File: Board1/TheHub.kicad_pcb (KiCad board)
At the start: 2 copper layers, 195.6 x 195.6 mm, 55 parts, among them J1 ARM_ADC_1, J10 SCIENCE + WHEELS POWER CONN, J11 RFD900, J12 I2C_1 Test Point, J13 I2C_2 Test Point, J14 ARDUINO NANO LEFT, J15 GPIO Test, J16 I2C_3 Test Point, J17 12V OUT, J18 7.4V IN, J19 ANALOG SENSORS, J2 ARM_ADC_2, J20 GPS, J21 COMPASS, J22 ARDUINO NANO RIGHT, J23 NucleoRight, J3 ARM_PWM_OUT, J4 ARM POWER CONN, J5 NucleoLeft, J6 SCI_ADC_1, J7 SCIENCE_PWM_OUT, J8 12V MAIN POWER, J9 WHEEL_ADC_1, U1 PRE-PCA9685, U2 PRE-ADS1115, U3 PRE-ADS1115, U4 PRE-PCA9685, U5 PRE-ADS1115, U6 TL1963, U7 LM340MP-5.0, U9 PRE-ADS1115

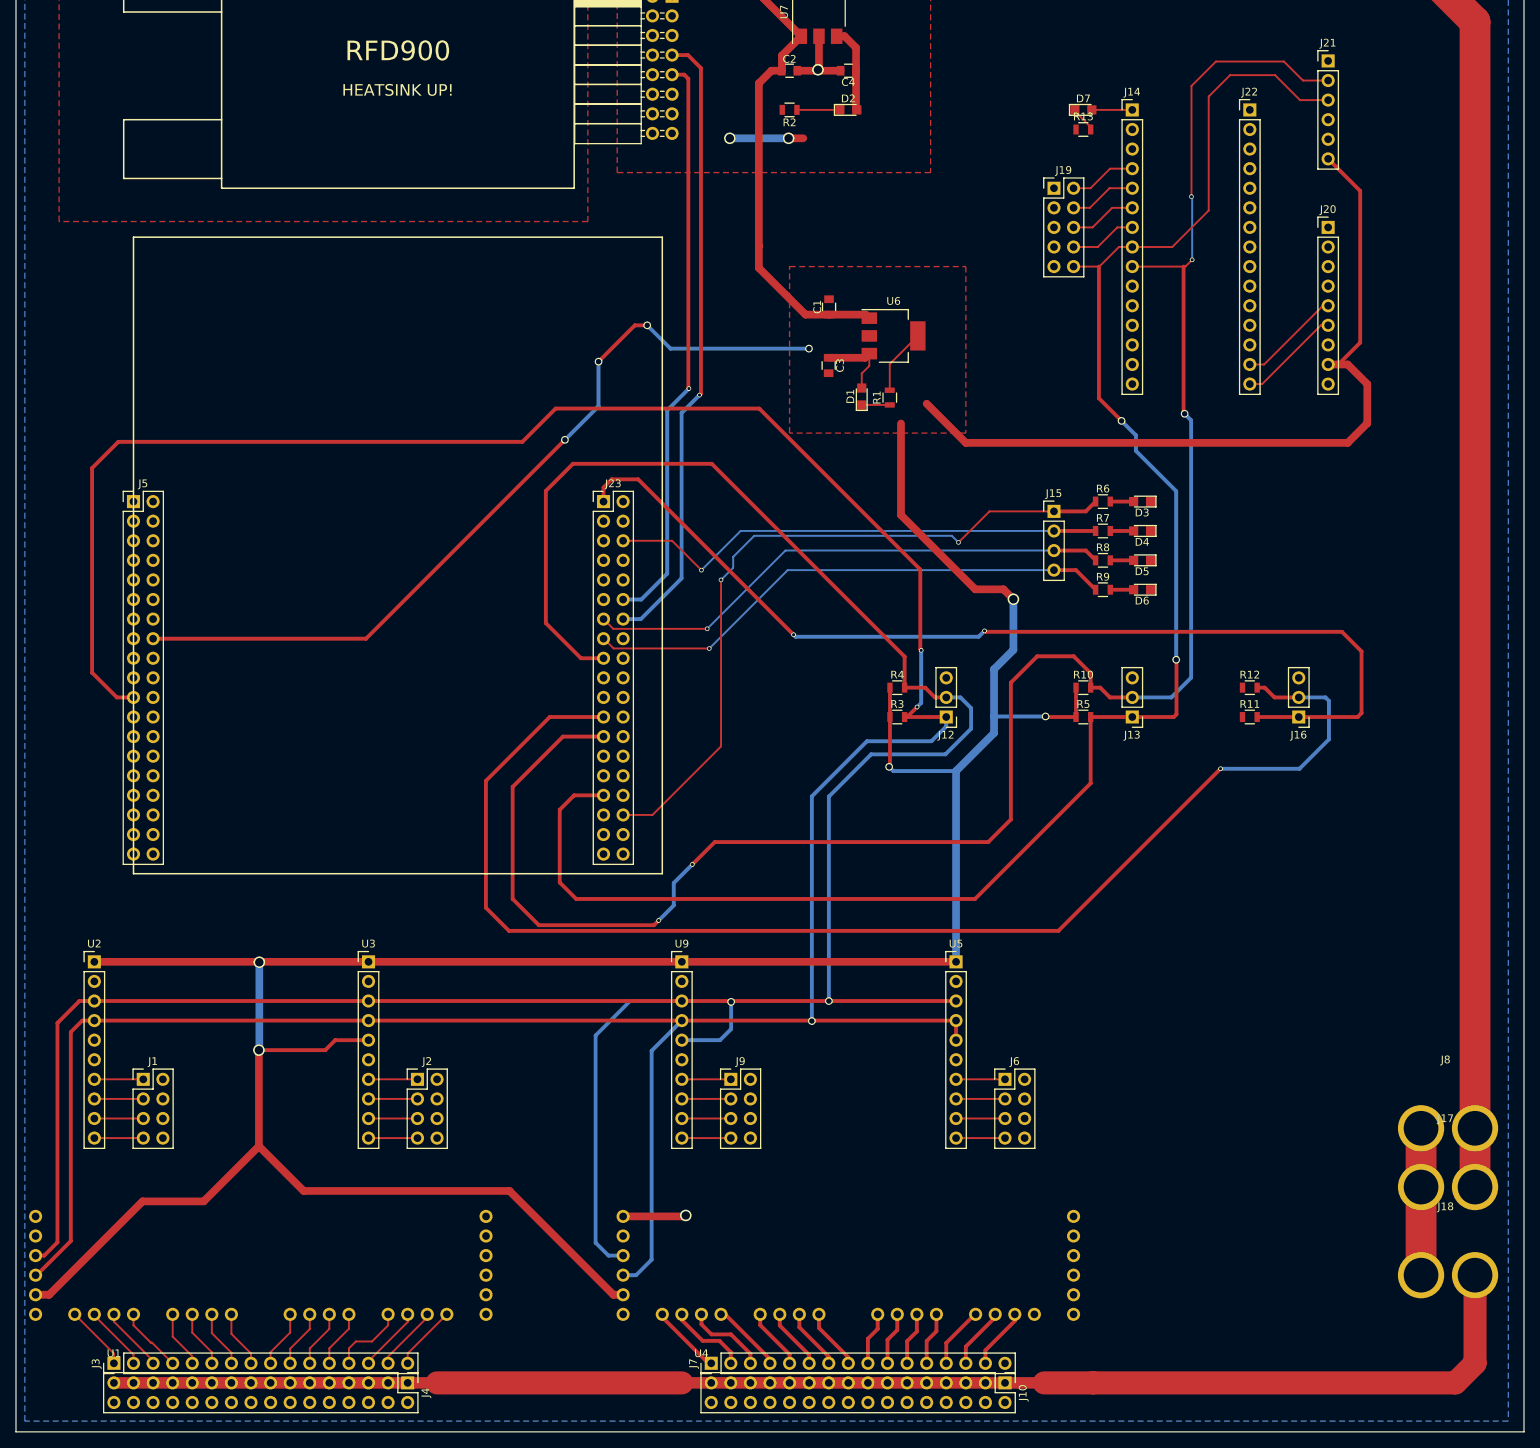
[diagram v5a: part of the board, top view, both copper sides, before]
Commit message: Add silkscreen labeling
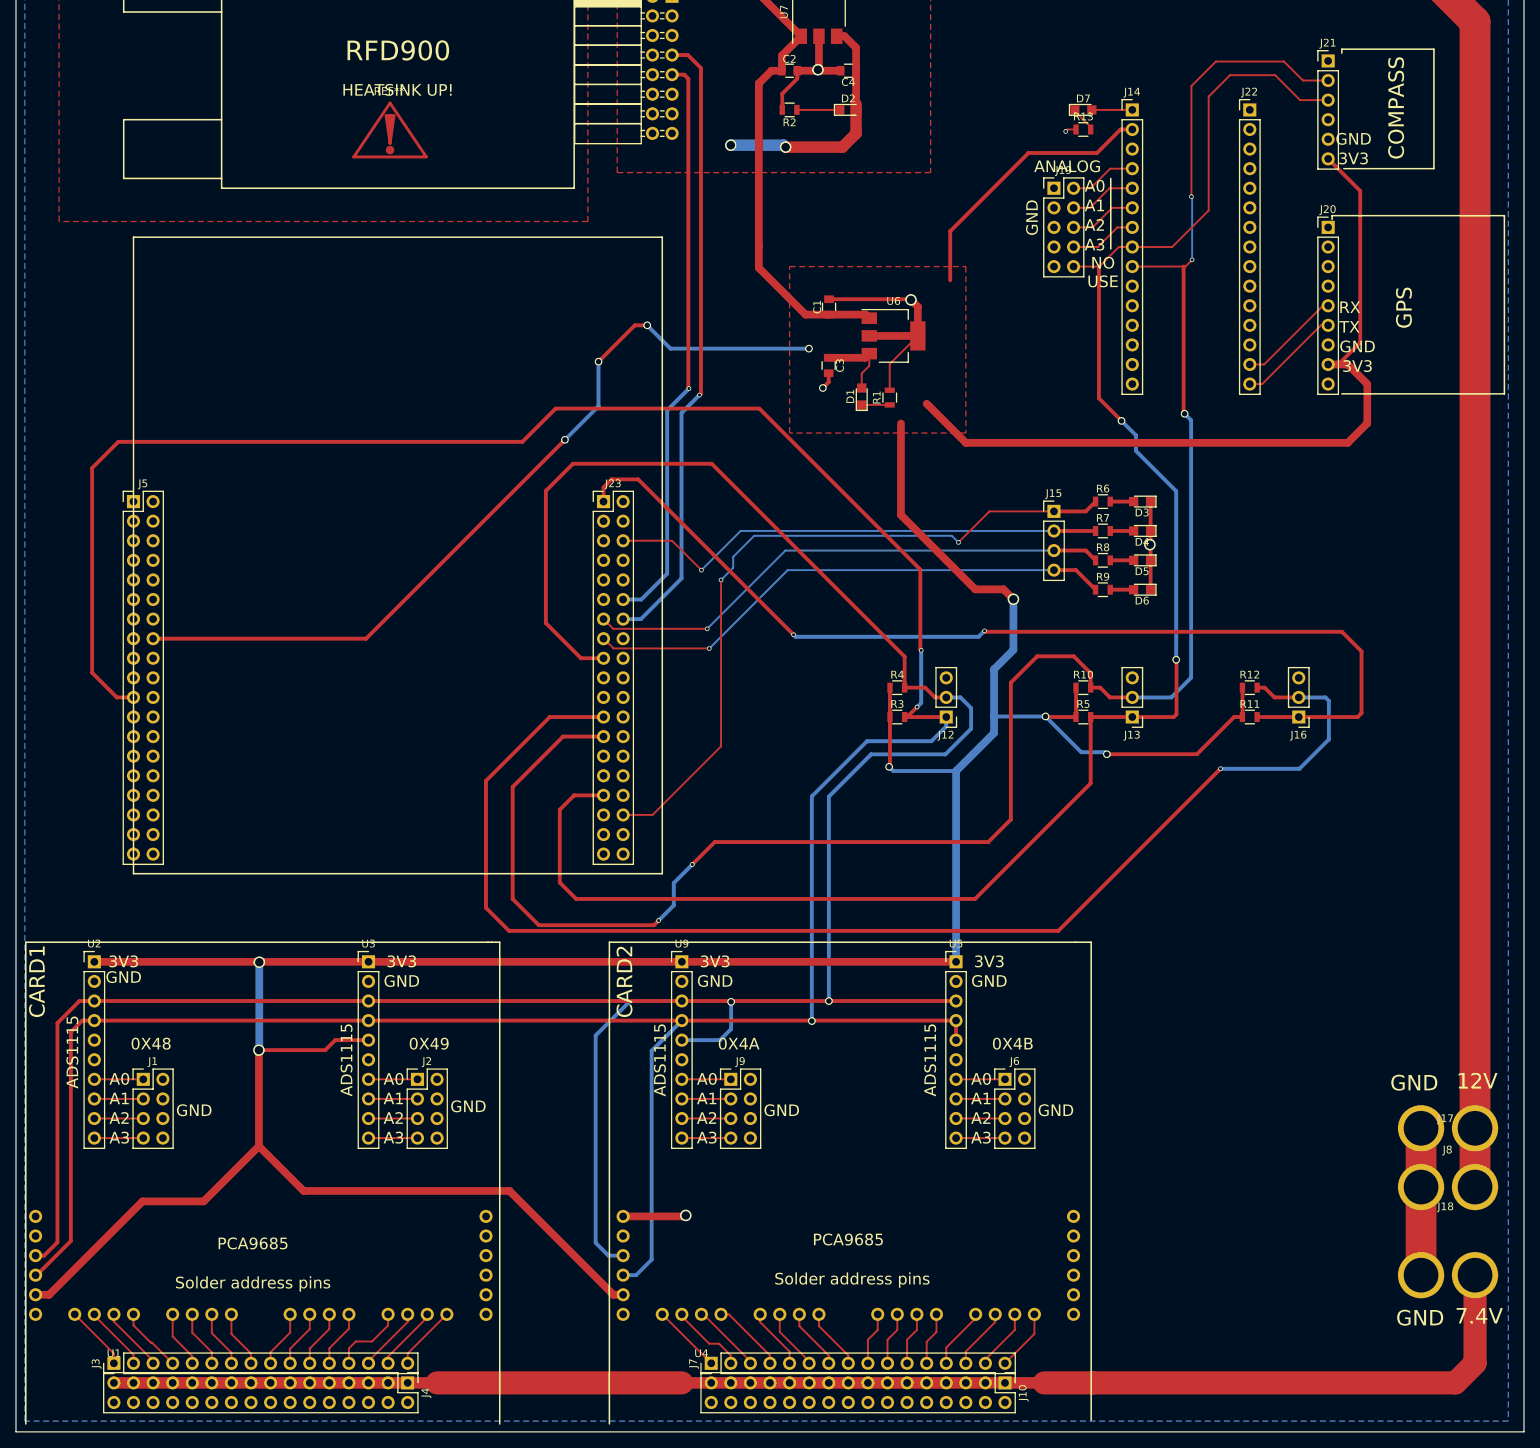
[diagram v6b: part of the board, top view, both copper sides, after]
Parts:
- added REF**: Symbol_Attention_CopperTop_Small, Symbols:Symbol_Attention_CopperTop_Small, F.Cu at (110.2, 77.7)
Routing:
- net +3V3: track 576.8 -> 645.6 mm, vias 9 -> 10
- net GND: track 45.9 -> 89.2 mm, vias 2 -> 6
- net +5V: track 20.8 -> 32.1 mm
- net Net-(J7-Pad16): track 0.00 -> 7.93 mm
- net Net-(J7-Pad3): track 10.5 -> 9.13 mm
- net Net-(J7-Pad2): track 10.3 -> 9.72 mm
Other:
- board text added: "0X48"
- board text added: "0X49"
- board text added: "0X4A"
- board text added: "0X4B"
- board text added: "12V"
- board text added: "3V3"
- board text added: "7.4V"
- board text added: "A0"
- board text added: "A1"
- board text added: "A2"
- board text added: "A3"
- board text added: "ADS1115"
- board text added: "ANALOG"
- board text added: "CARD1"
- board text added: "CARD2"
- board text added: "COMPASS"
- board text added: "GND"
- board text added: "GPS"
- board text added: "NO USE"
- board text added: "PCA9685"
- board text added: "RX"
- board text added: "Solder address pins"
- board text added: "TX"
